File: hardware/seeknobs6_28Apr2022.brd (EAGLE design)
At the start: 162.6 x 25.4 mm, 29 parts, among them SW1 SPST-6.0MM, SW2 SPST-6.0MM, SW3 SPST-6.0MM, SW4 SPST-6.0MM

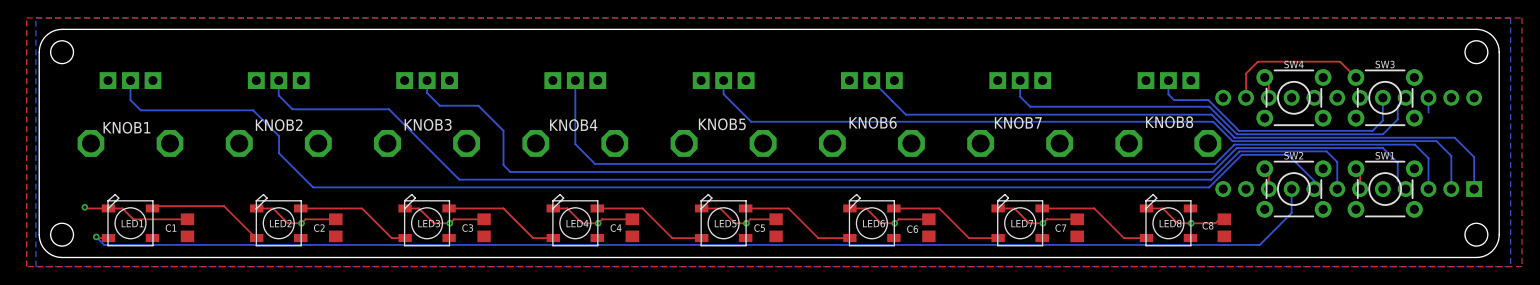
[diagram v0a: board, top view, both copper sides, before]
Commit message: doc updates, cirpy example
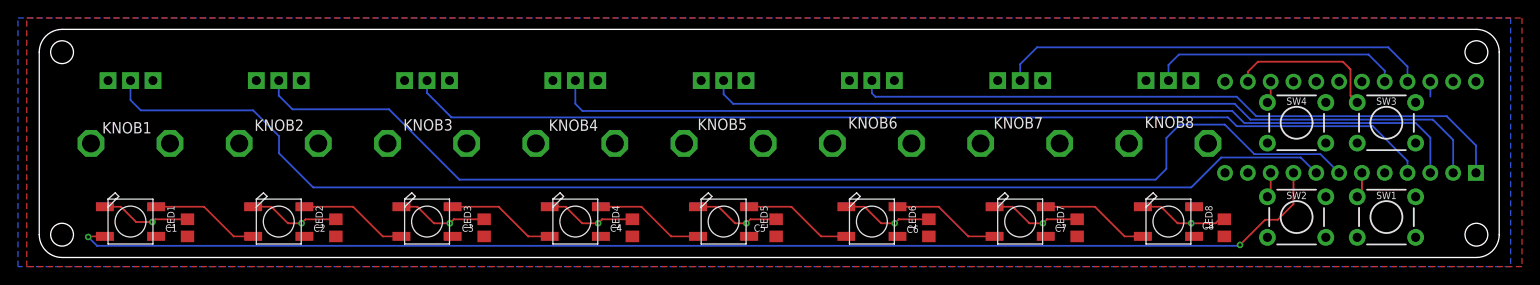
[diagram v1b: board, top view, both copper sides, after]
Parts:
- LED1, LED2, LED3, LED4, LED5, LED6, LED7, LED8: value MICROBUILDER_WS2812B5050 -> WS2812B5050EZ; device Adafruit MacroPad 2040:MICROBUILDER_WS2812B -> todstuff:WS2812B-EASY
- moved SW2 3.13 mm to (140.0, 4.50)
- moved SW1 3.12 mm to (150.0, 4.50)
- moved SW4 2.80 mm to (140.0, 15.0)
- moved SW3 2.78 mm to (150.0, 15.0)
- moved SEESAW 1.81 mm to (146.0, 14.5)
- moved LED1 0.19 mm to (10.2, 4.00)
- moved LED2 0.19 mm to (26.7, 4.00)
- moved LED3 0.19 mm to (43.2, 4.00)
- moved LED4 0.19 mm to (59.7, 4.00)
- moved LED5 0.19 mm to (76.2, 4.00)
- moved LED6 0.19 mm to (92.7, 4.00)
- moved LED7 0.19 mm to (109.2, 4.00)
- moved LED8 0.19 mm to (125.7, 4.00)
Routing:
- net KNOB3: track 120.4 -> 115.0 mm
- net KNOB4: track 107.9 -> 103.3 mm
- net NEOPIXEL: track 139.0 -> 141.9 mm, vias 1 -> 2
- net KNOB2: track 128.2 -> 130.4 mm
- net KNOB8: track 30.1 -> 28.3 mm
- net GND: track 80.7 -> 82.1 mm
- net KNOB1: track 142.7 -> 141.4 mm
- net SW3: track 16.2 -> 17.3 mm
- net N$3: track 13.2 -> 12.2 mm
- net N$7: track 13.0 -> 12.2 mm
- net N$6: track 13.0 -> 12.2 mm
- net N$4: track 13.0 -> 12.2 mm
- net N$1: track 13.0 -> 12.2 mm
- net N$2: track 13.0 -> 12.2 mm
- net N$5: track 13.0 -> 12.2 mm
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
